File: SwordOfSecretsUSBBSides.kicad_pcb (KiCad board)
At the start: 2 copper layers, 68.3 x 131.7 mm, 37 parts, among them J1 DebugEdge_02x05, J2 USB_A, J5 Conn_01x03_Pin, SW1 SW_Push, SW2 SW_Push, SW3 SW_Push, U2 AMS1117-3.3, U3 W25Q128JVS, U4 CH32V003F4P6, U5 CH340E

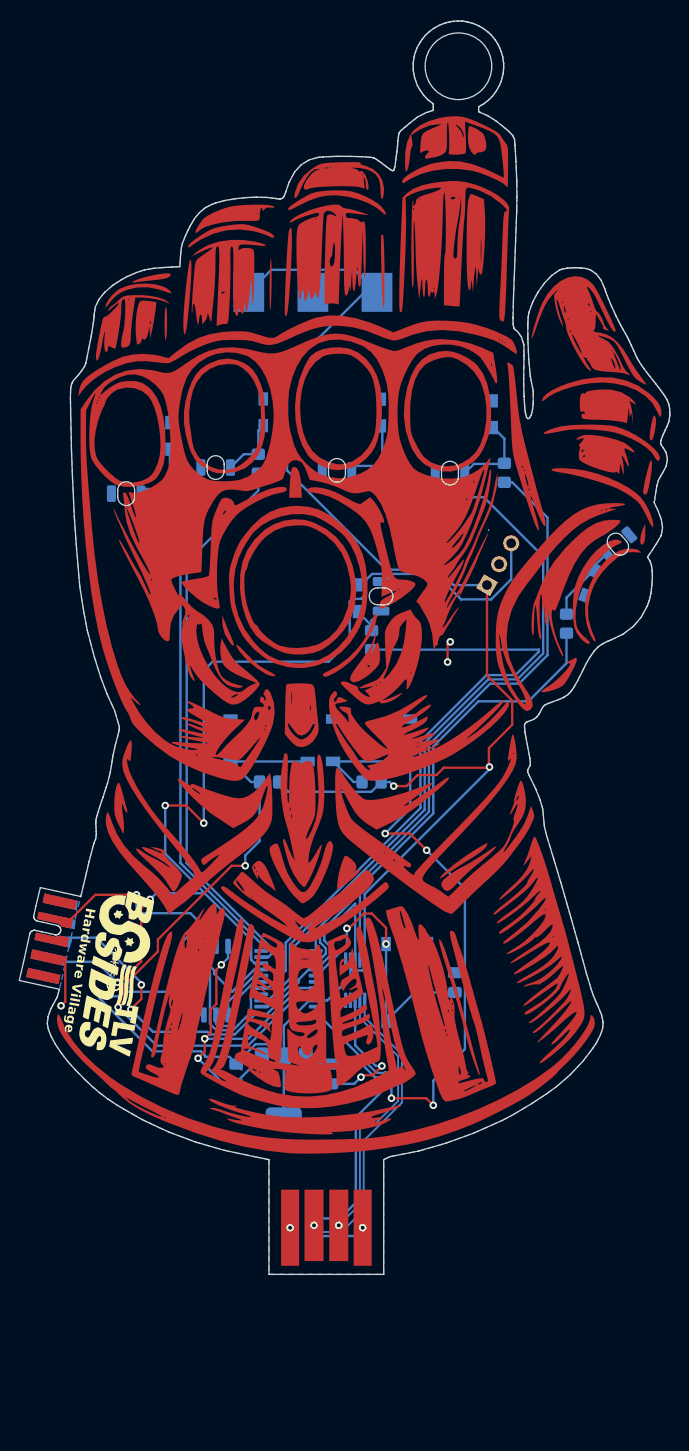
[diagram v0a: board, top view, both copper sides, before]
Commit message: Fixing debug edge to include UART, adding protection diodes to 3.3v lines from battery and LDO and adding boost converter to ensure 3.3v from battery
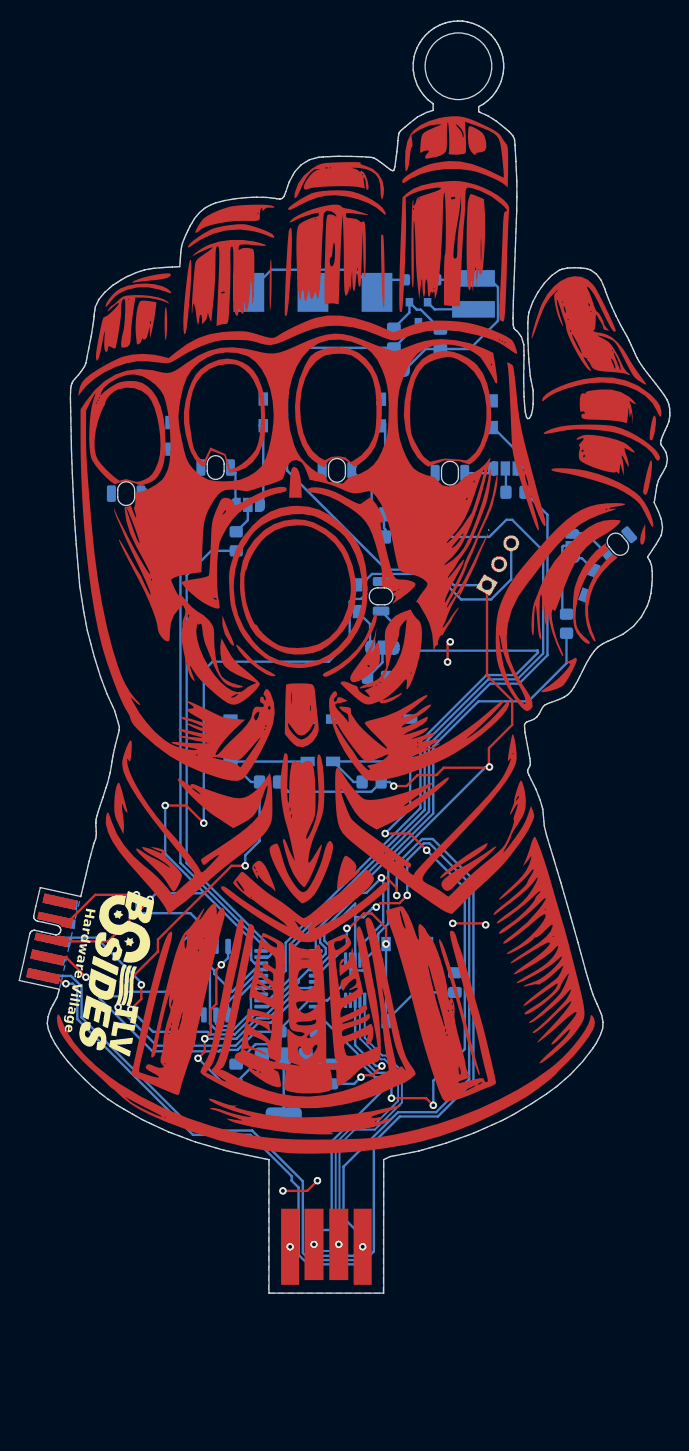
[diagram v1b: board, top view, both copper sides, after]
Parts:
- added C4: 100uF, Capacitor_SMD:C_0805_2012Metric_Pad1.18x1.45mm_HandSolder, B.Cu at (3.07, -20.3)
- added C5: 100uF, Capacitor_SMD:C_0805_2012Metric_Pad1.18x1.45mm_HandSolder, B.Cu at (7.95, -20.2)
- added D13: D, Diode_SMD:D_SOD-123, B.Cu at (-6.98, 52.6)
- added D14: D, Diode_SMD:D_SOD-123, B.Cu at (5.97, -26.4)
- added JP1: SolderJumper_3_Open, SolderJumper:SolderJumper-3_P1.3mm_Open_RoundedPad1.0x1.5mm_NumberLabels, B.Cu at (-19.8, -2.70)
- added JP2: SolderJumper_3_Open, SolderJumper:SolderJumper-3_P1.3mm_Open_RoundedPad1.0x1.5mm_NumberLabels, B.Cu at (-12.3, -2.78)
- added JP3: SolderJumper_3_Open, SolderJumper:SolderJumper-3_P1.3mm_Open_RoundedPad1.0x1.5mm_NumberLabels, B.Cu at (2.03, -1.79)
- added JP4: SolderJumper_3_Open, SolderJumper:SolderJumper-3_P1.3mm_Open_RoundedPad1.0x1.5mm_NumberLabels, B.Cu at (14.8, -6.60)
- added JP5: SolderJumper_3_Open, SolderJumper:SolderJumper-3_P1.3mm_Open_RoundedPad1.0x1.5mm_NumberLabels, B.Cu at (21.8, 1.52)
- added JP6: SolderJumper_3_Open, SolderJumper:SolderJumper-3_P1.3mm_Open_RoundedPad1.0x1.5mm_NumberLabels, B.Cu at (1.87, 12.2)
- added JP7: SolderJumper_2_Open, SolderJumper:SolderJumper-2_P1.3mm_Open_RoundedPad1.0x1.5mm, B.Cu at (3.59, -17.0)
- added L1: 47uH, Inductor_SMD:L_Ferrocore_DLG-0403, B.Cu at (11.4, -24.9)
- added U1: ~, QX2304L33T:QX2304L33T, B.Cu at (5.65, -23.1)
- moved R3 8.48 mm to (-13.5, 1.05)
- moved R4 6.60 mm to (3.17, 0.59), turned to 180 degrees
- moved R2 4.47 mm to (-19.8, 0.98)
- moved R1 3.96 mm to (1.30, 15.3), turned to 180 degrees
- moved R5 2.36 mm to (15.8, -4.10), turned to 180 degrees
- moved J2 2.00 mm to (-4.02, 80.0)
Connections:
- BT1 pad 1: 3.3v -> Net-(BT1-+)
- C2 pad 2: 3.3v -> Net-(D13-A)
- D4 pad 2: Net-(D10-A) -> Net-(D4-A)
- D5 pad 2: Net-(D11-A) -> Net-(D5-A)
- D6 pad 2: Net-(D12-A) -> Net-(D6-A)
- D7 pad 2: Net-(D1-A) -> Net-(D7-A)
- D8 pad 2: Net-(D2-A) -> Net-(D8-A)
- D9 pad 2: Net-(D3-A) -> Net-(D9-A)
- J1 pad 10: TRACE1 -> RX
- J1 pad 2: unconnected-(J1-SWDIO/TMS-Pad2) -> SWIO
- J1 pad 6: SWIO -> unconnected-(J1-SWO/TDO-Pad6)
- J1 pad 9: TRACE0 -> RXOUT
- R1 pad 2: Net-(D1-A) -> Net-(JP6-C)
- R2 pad 2: Net-(D2-A) -> Net-(JP1-C)
- R3 pad 2: Net-(D3-A) -> Net-(JP2-C)
- R4 pad 2: Net-(D10-A) -> Net-(JP3-C)
- R5 pad 2: Net-(D11-A) -> Net-(JP4-C)
- R6 pad 2: Net-(D12-A) -> Net-(JP5-C)
- U2 pad 2: 3.3v -> Net-(D13-A)
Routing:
- net RXOUT: track 16.6 -> 139.1 mm, vias 0 -> 3
- net RX: track 14.8 -> 134.8 mm, vias 0 -> 2
- net Net-(BT1-+): track 0.00 -> 22.3 mm
- net Net-(D14-K): track 0.00 -> 22.2 mm
- net 3.3v: track 228.8 -> 207.4 mm
- net Net-(D13-A): track 0.00 -> 17.7 mm
- net GND: track 60.0 -> 73.2 mm, vias 9 -> 13
- net Net-(D4-A): track 0.00 -> 10.3 mm
- net Net-(JP5-C): track 0.00 -> 8.38 mm
- net PD2: track 58.5 -> 50.9 mm
- net Net-(D11-A): track 9.47 -> 3.17 mm
- net SWIO: track 111.5 -> 105.8 mm, vias 4 -> 3
- net Net-(D5-A): track 0.00 -> 5.37 mm
- net Net-(U1-LX): track 0.00 -> 5.14 mm
- net PD3: track 50.5 -> 45.8 mm
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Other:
- board size 68.3 x 131.7 mm -> 68.3 x 133.6 mm
- board text added: "Bridge Battery"

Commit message: Changed battery, fixed side-mouted LED orientation
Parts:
- removed BT1: Battery_Cell, Battery:MY-1025-01
- removed C4, C5: 100uF, Capacitor_SMD:C_0805_2012Metric_Pad1.18x1.45mm_HandSolder
- removed JP7: SolderJumper_2_Open, SolderJumper:SolderJumper-2_P1.3mm_Open_RoundedPad1.0x1.5mm
- removed L1: 47uH, Inductor_SMD:L_Ferrocore_DLG-0403
- removed U1: ~, QX2304L33T:QX2304L33T
- added J3: Conn_01x02_Pin, Connector_PinHeader_2.54mm:PinHeader_1x02_P2.54mm_Vertical, F.Cu at (-11.7, -22.1)
- C2, C3: footprint Capacitor_SMD:C_0805_2012Metric_Pad1.18x1.45mm_HandSolder -> Capacitor_SMD:C_1206_3216Metric_Pad1.33x1.80mm_HandSolder
- moved D14 12.8 mm to (-5.85, -21.6), turned to 90 degrees
- moved C3 2.66 mm to (-3.45, 59.7), turned to 90 degrees
- moved C2 2.61 mm to (-13.6, 59.6), turned to -90 degrees
- turned D1 to 90 degrees
- turned D2 to 90 degrees
- turned D3 to 90 degrees
- turned D4 to 90 degrees
- turned D5 to 90 degrees
- turned D6 to -110 degrees
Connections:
- D14 pad 1: Net-(D14-K) -> 3.3v
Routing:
- net Net-(D14-K): track 22.2 -> 0.00 mm
- net GND: track 73.2 -> 93.3 mm
- net Net-(D14-A): track 22.3 -> 3.79 mm
- net 3.3v: track 207.4 -> 193.0 mm
- net Net-(U1-LX): track 5.14 -> 0.00 mm
- net PC2: track 78.4 -> 81.8 mm
- net Net-(D3-A): track 8.88 -> 11.9 mm
- net VCC: track 38.2 -> 41.0 mm
- net Net-(D2-A): track 6.72 -> 9.52 mm
- net Net-(D1-A): track 4.33 -> 7.13 mm
- net Net-(D5-A): track 5.37 -> 8.17 mm
- net Net-(D4-A): track 10.3 -> 13.1 mm
- net Net-(D13-A): track 17.7 -> 16.4 mm
- net Net-(D6-A): track 3.16 -> 4.43 mm
- net SWIO: track 105.8 -> 106.0 mm, vias 3 -> 5

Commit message: Production fixes
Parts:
- added BT1: BATTERY-AAA, Battery:BH-AAA-A1AJ001, B.Cu at (-20.8, 29.9)
- added BT2: BATTERY-AAA, Battery:BH-AAA-A1AJ001, B.Cu at (10.4, 30.8)
- added G***: LOGO, LOGO, F.Cu at (-4.06, 87.2)
- added mouse-bite-2.54mm-slot: VAL**, Panelization:mouse-bite-2.54mm-slot, F.Cu at (-4.05, 81.3)
- J3: moved to B.Cu
- moved SW1 12.1 mm to (-6.00, 32.0)
- moved R7 11.9 mm to (-5.80, 36.3)
- moved JP6 8.51 mm to (-6.40, 14.2)
- moved R1 7.97 mm to (-6.55, 16.7)
- moved C1 7.61 mm to (4.55, 53.2), turned to 0 degrees
- moved D7 5.93 mm to (-1.18, 1.66), turned to -60 degrees
- moved R8 4.24 mm to (-5.80, 26.3)
- moved SW3 4.04 mm to (-6.00, 22.0)
- moved U3 1.45 mm to (-14.8, 47.2)
- moved G*** 1.24 mm to (-26.6, 45.0), turned to 70 degrees
- moved D1 0.08 mm to (-0.82, 7.00)
- turned J3 to -90 degrees
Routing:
- net 3.3v: track 193.0 -> 224.0 mm
- net Net-(BT1--): track 0.00 -> 22.2 mm
- net Net-(D7-A): track 4.43 -> 22.7 mm
- net Net-(D1-A): track 7.13 -> 23.9 mm
- net GND: track 93.3 -> 82.6 mm, vias 13 -> 12
- net PC4: track 66.5 -> 74.9 mm
- net RST: track 67.7 -> 59.7 mm
- net PC0: track 73.8 -> 68.0 mm
- net MOSI: track 6.00 -> 10.1 mm
- net MISO: track 10.0 -> 6.03 mm
- net SCK: track 8.98 -> 5.27 mm
- net RX: track 134.8 -> 136.6 mm
- net RXOUT: track 139.1 -> 140.3 mm
- net SWIO: track 106.0 -> 107.0 mm
- net Net-(JP6-C): track 3.78 -> 2.98 mm
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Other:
- board size 68.3 x 133.6 mm -> 68.3 x 148.2 mm
- board text added: "Break Me!"

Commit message: Fixing according to comments
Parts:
- removed J1: DebugEdge_02x05, DebugEdge_2x05_Target:DebugEdge_2x05_Target
- moved G*** 2.00 mm to (-26.9, 43.1)
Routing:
- net SWIO: track 107.0 -> 94.7 mm
- net 3.3v: track 224.0 -> 217.2 mm
- net GND: track 82.6 -> 77.3 mm
- net RST: track 59.7 -> 55.3 mm
- net RX: track 136.6 -> 133.6 mm
- net RXOUT: track 140.3 -> 137.9 mm
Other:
- board size 68.3 x 148.2 mm -> 65.4 x 148.2 mm
- board text added: "2025"

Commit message: Updating 2nd Eng Board revision
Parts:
- moved D7 3.32 mm to (-3.41, -0.80), turned to -50 degrees
- moved D1 2.24 mm to (-1.02, 4.77)
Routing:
- net RX: track 133.6 -> 121.8 mm
- net 3.3v: track 217.2 -> 207.3 mm, vias 3 -> 2
- net RXOUT: track 137.9 -> 128.4 mm, vias 3 -> 2
- net SWIO: track 94.7 -> 88.7 mm, vias 5 -> 4
- net Net-(D7-A): track 22.7 -> 26.0 mm
- net RST: track 55.3 -> 57.9 mm
- net Net-(D1-A): track 23.9 -> 25.0 mm
- net GND: vias 12 -> 11
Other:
- board text added: "Btn0"
- board text added: "Btn1"
- board text added: "RST"
- board text added: "Rx"
- board text added: "Tx"

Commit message: WIP Production-ready files
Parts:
- removed D10, D11, D12, D7, D8, D9: LED, LED_SMD:LED_1206_3216Metric_ReverseMount_Hole1.8x2.4mm
- removed JP1, JP2, JP3, JP4, JP5, JP6: SolderJumper_3_Open, SolderJumper:SolderJumper-3_P1.3mm_Open_RoundedPad1.0x1.5mm_NumberLabels
- C1: value C -> 100nF
- C2, C3: value C -> 100uF
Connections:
- R1 pad 2: Net-(JP6-C) -> Net-(D1-A)
- R2 pad 2: Net-(JP1-C) -> Net-(D2-A)
- R3 pad 2: Net-(JP2-C) -> Net-(D3-A)
- R4 pad 2: Net-(JP3-C) -> Net-(D4-A)
- R5 pad 2: Net-(JP4-C) -> Net-(D5-A)
- R6 pad 2: Net-(JP5-C) -> Net-(D6-A)
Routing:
- net Net-(D7-A): track 26.0 -> 0.00 mm
- net Net-(JP5-C): track 8.38 -> 0.00 mm
- net GND: track 77.3 -> 70.5 mm
- net Net-(D10-A): track 6.22 -> 0.00 mm
- net Net-(D12-A): track 4.45 -> 0.00 mm
- net Net-(D3-A): track 11.9 -> 15.8 mm
- net Net-(D9-A): track 3.69 -> 0.00 mm
- net Net-(JP2-C): track 3.34 -> 0.00 mm
- net Net-(D8-A): track 3.27 -> 0.00 mm
- net Net-(D2-A): track 9.52 -> 12.7 mm
- net Net-(D11-A): track 3.17 -> 0.00 mm
- net Net-(D5-A): track 8.17 -> 11.2 mm
- net Net-(JP6-C): track 2.98 -> 0.00 mm
- net Net-(JP1-C): track 2.68 -> 0.00 mm
- net Net-(D1-A): track 25.0 -> 27.6 mm
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
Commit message: Almost final production files
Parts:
- moved D2 0.59 mm to (-21.0, -10.0)
- moved D4 0.34 mm to (1.42, -12.5)
- moved D5 0.21 mm to (13.3, -12.3)
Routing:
- net GND: track 70.5 -> 61.9 mm
- net Net-(D2-A): track 12.7 -> 13.3 mm
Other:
- outline, holes or cut-outs redrawn

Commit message: chore: Updating to the latest PCB layout
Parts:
- removed mouse-bite-2.54mm-slot: VAL**, Panelization:mouse-bite-2.54mm-slot
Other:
- board size 65.4 x 148.2 mm -> 65.4 x 133.6 mm
